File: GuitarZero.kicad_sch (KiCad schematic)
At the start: 2 parts, among them J1 AudioJack2_Ground, J2 USB_B_Micro

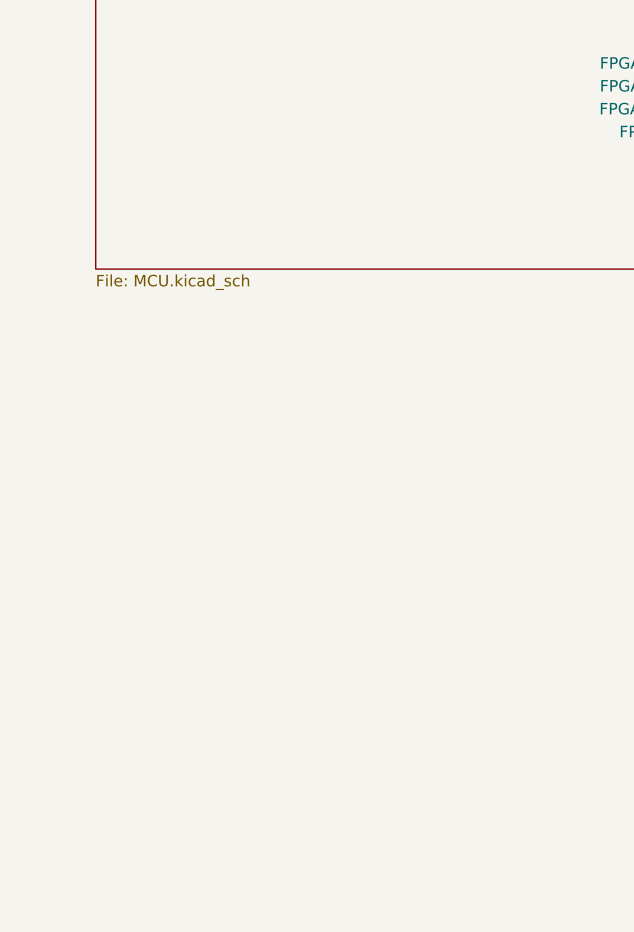
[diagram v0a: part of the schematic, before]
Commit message: Added buttons and connected them to the MCU
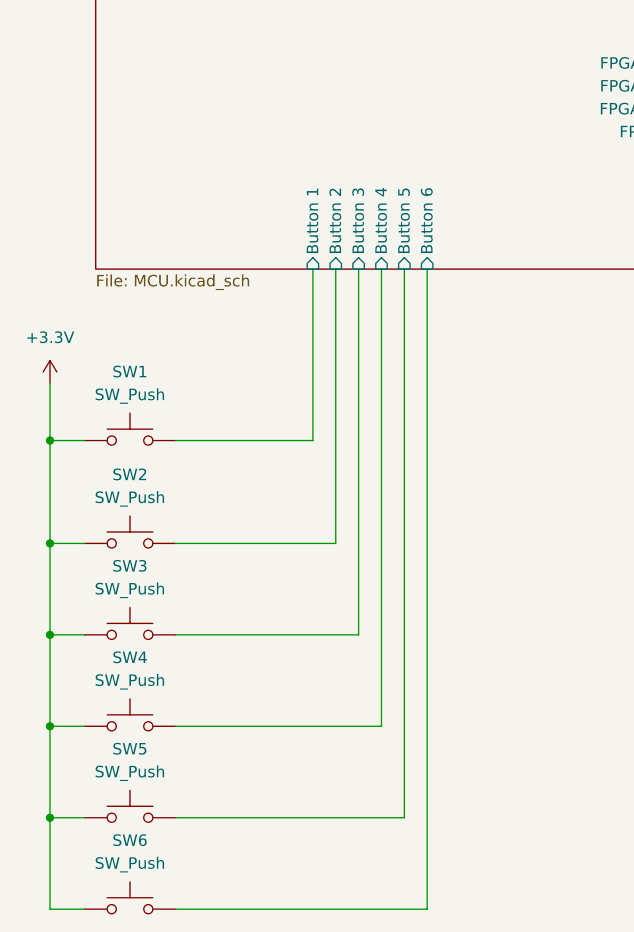
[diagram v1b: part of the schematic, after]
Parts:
- added SW1, SW2, SW3, SW4, SW5, SW6: SW_Push, symbol Switch:SW_Push
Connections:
- net +3.3V: now also SW1.1, SW2.1, SW3.1, SW4.1, SW5.1, SW6.1
- new net MCU/Button 1: SW1.2
- new net MCU/Button 2: SW2.2
- new net MCU/Button 3: SW3.2
- new net MCU/Button 4: SW4.2
- new net MCU/Button 5: SW5.2
- new net MCU/Button 6: SW6.2
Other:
- sheet MCU ports: added Button 1, Button 2, Button 3, Button 4, Button 5, Button 6; removed none

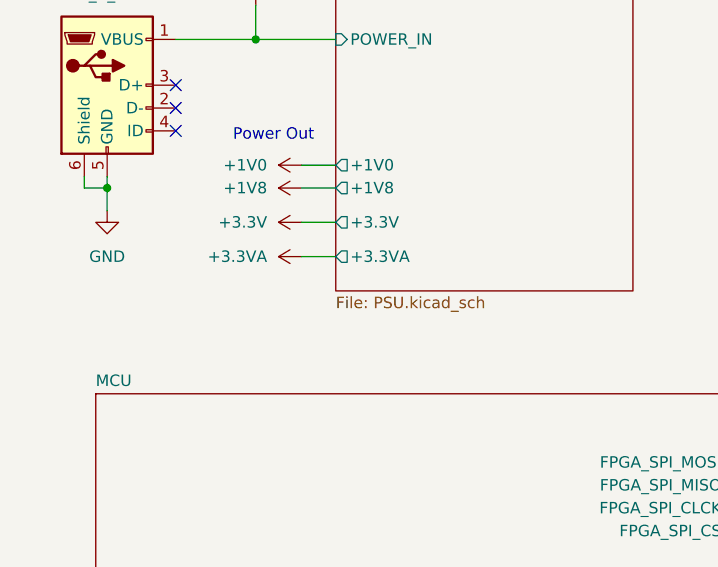
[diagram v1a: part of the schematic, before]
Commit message: Resolved some Electrial Rules
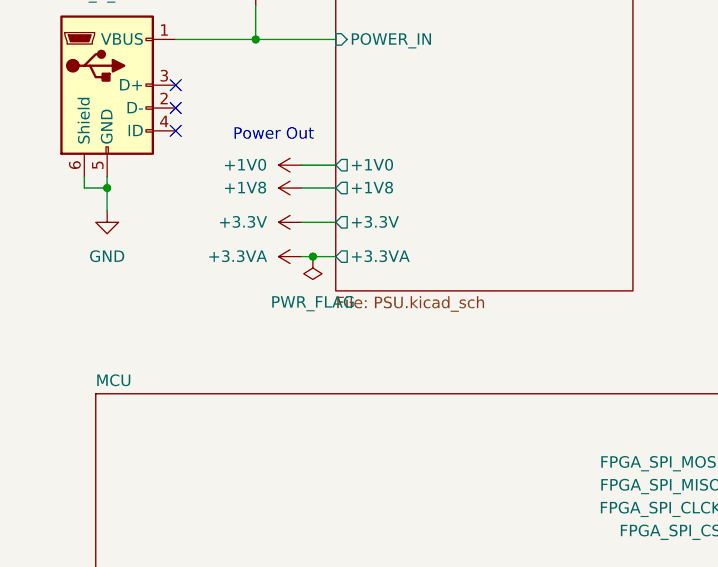
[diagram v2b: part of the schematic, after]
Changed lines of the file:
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@@
 (kicad_sch (version 20230121) (generator eeschema)
   (paper "A4")
+  (junction (at 53.34 55.88) (diameter 0) (color 0 0 0 0)
+  )
   (junction (at 24.13 120.65) (diameter 0) (color 0 0 0 0)
   )
@@
     (stroke (width 0) (type default))
   )
-  (wire (pts (xy 52.07 55.88) (xy 55.88 55.88))
+  (wire (pts (xy 52.07 55.88) (xy 53.34 55.88))
     (stroke (width 0) (type default))
   )
@@
   )
   (wire (pts (xy 55.88 132.08) (xy 55.88 101.6))
+    (stroke (width 0) (type default))
+  )
+  (wire (pts (xy 53.34 55.88) (xy 55.88 55.88))
     (stroke (width 0) (type default))
   )
@@
         )
       )
+    )
+  )
+  (symbol (lib_id "power:PWR_FLAG") (at 53.34 55.88 180) (unit 1)
+    (in_bom yes) (on_board yes) (dnp no) (fields_autoplaced)
+    (property "Reference" "#FLG01" (at 53.34 57.785 0)
+      (effects (font (size 1.27 1.27)) hide)
+    )
+    (property "Value" "PWR_FLAG" (at 53.34 60.96 0)
+      (effects (font (size 1.27 1.27)))
+    )
+    (property "Footprint" "" (at 53.34 55.88 0)
+      (effects (font (size 1.27 1.27)) hide)
+    )
+    (property "Datasheet" "~" (at 53.34 55.88 0)
+      (effects (font (size 1.27 1.27)) hide)
+    )
+    (pin "1")
+    (instances
+      (project "GuitarZero"
+        (path "/fba50eda-8593-4456-af98-ff56fd418a76"
+          (reference "#FLG01") (unit 1)
+        )
+      )

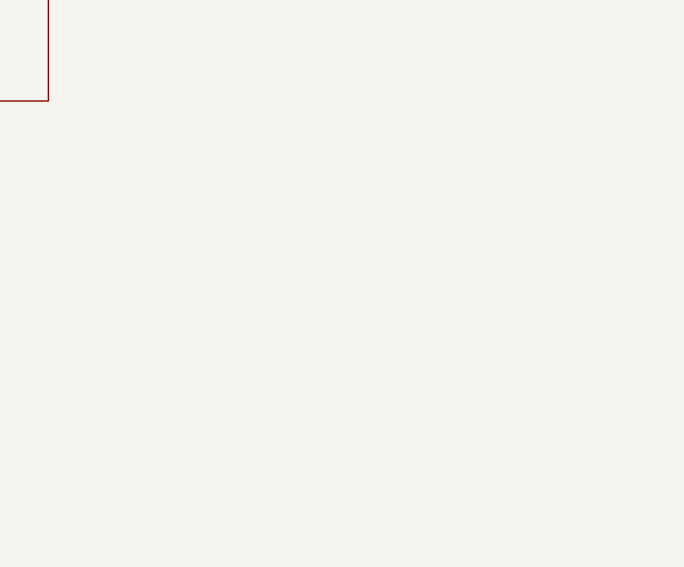
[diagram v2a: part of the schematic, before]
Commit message: Added DAC schematic
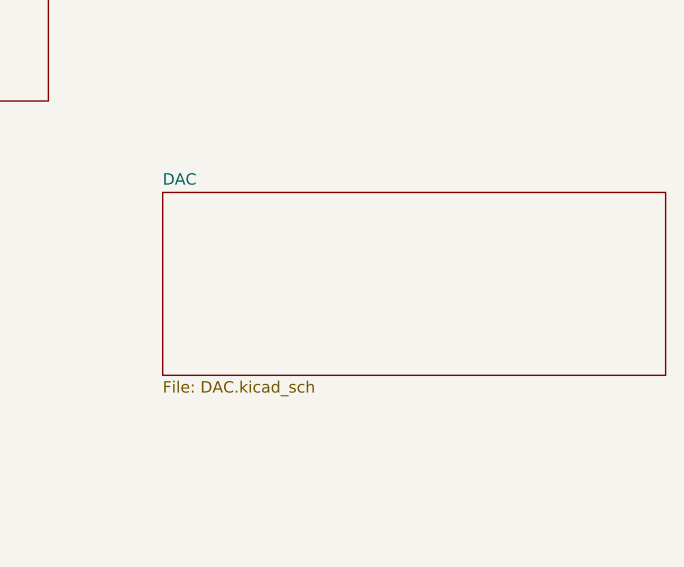
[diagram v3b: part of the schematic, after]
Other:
- added sheet DAC (DAC.kicad_sch)
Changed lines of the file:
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@@
+    )
+  )
+  (sheet (at 198.12 69.85) (size 55.88 20.32) (fields_autoplaced)
+    (stroke (width 0.1524) (type solid))
+    (fill (color 0 0 0 0.0000))
+    (property "Sheetname" "DAC" (at 198.12 69.1384 0)
+      (effects (font (size 1.27 1.27)) (justify left bottom))
+    )
+    (property "Sheetfile" "DAC.kicad_sch" (at 198.12 90.7546 0)
+      (effects (font (size 1.27 1.27)) (justify left top))
+    )
+    (instances
+      (project "GuitarZero"
+        (path "/fba50eda-8593-4456-af98-ff56fd418a76" (page "6"))
+      )
     )
   )

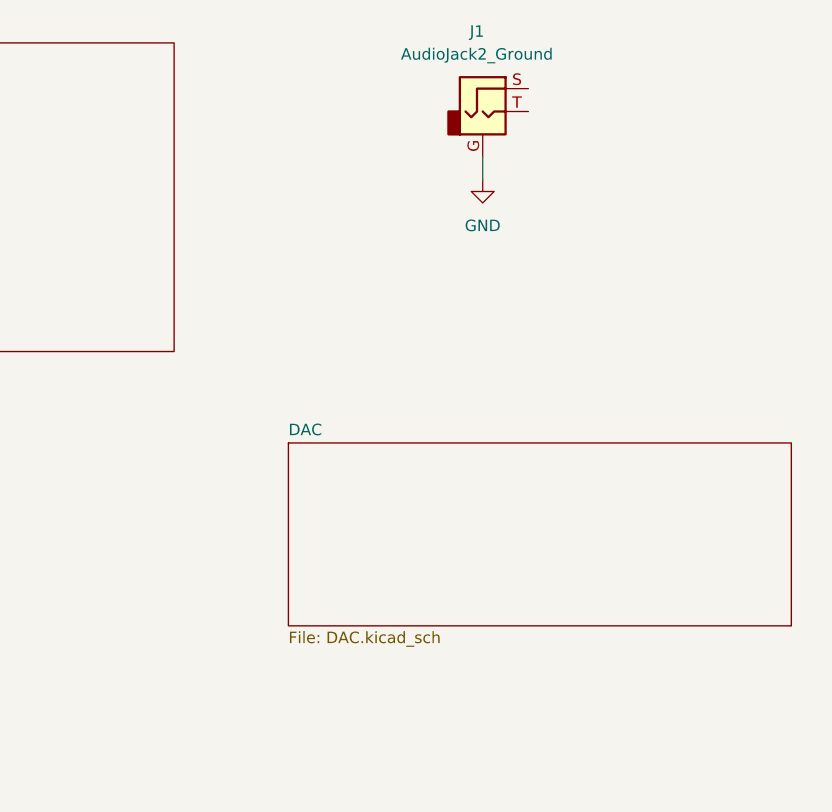
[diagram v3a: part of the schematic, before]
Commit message: Changed JACK and Speaker symbol
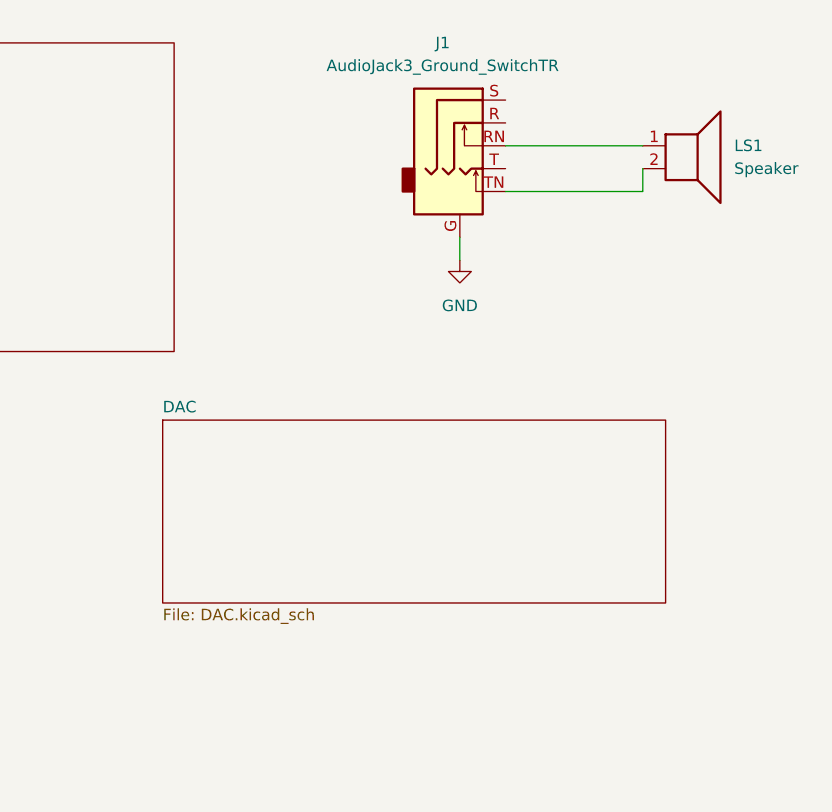
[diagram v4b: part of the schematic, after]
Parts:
- removed J1: AudioJack2_Ground, symbol Connector_Audio:AudioJack2_Ground
- added J1: AudioJack3_Ground_SwitchTR, symbol Connector_Audio:AudioJack3_Ground_SwitchTR
- added LS1: Speaker, symbol Device:Speaker
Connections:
- net GND: now also J1.G
- new net: J1.RN, LS1.1
- new net: J1.TN, LS1.2
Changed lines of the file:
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@@
+    (stroke (width 0) (type default))
+  )
+  (wire (pts (xy 237.49 41.91) (xy 237.49 39.37))
     (stroke (width 0) (type default))
   )
@@
     (stroke (width 0) (type default))
   )
+  (wire (pts (xy 222.25 41.91) (xy 237.49 41.91))
+    (stroke (width 0) (type default))
+  )
   (wire (pts (xy 24.13 120.65) (xy 24.13 132.08))
     (stroke (width 0) (type default))
@@
     (stroke (width 0) (type default))
   )
-  (wire (pts (xy 219.71 38.1) (xy 219.71 40.64))
+  (wire (pts (xy 217.17 46.99) (xy 217.17 49.53))
     (stroke (width 0) (type default))
   )
@@
   )
   (wire (pts (xy 24.13 142.24) (xy 24.13 152.4))
+    (stroke (width 0) (type default))
+  )
+  (wire (pts (xy 222.25 36.83) (xy 237.49 36.83))
     (stroke (width 0) (type default))
   )
@@
     )
   )
-  (symbol (lib_id "power:GND") (at 219.71 40.64 0) (unit 1)
-    (in_bom yes) (on_board yes) (dnp no) (fields_autoplaced)
-    (property "Reference" "#PWR033" (at 219.71 46.99 0)
-      (effects (font (size 1.27 1.27)) hide)
-    )
-    (property "Value" "GND" (at 219.71 45.72 0)
-      (effects (font (size 1.27 1.27)))
-    )
-    (property "Footprint" "" (at 219.71 40.64 0)
-      (effects (font (size 1.27 1.27)) hide)
-    )
-    (property "Datasheet" "" (at 219.71 40.64 0)
+  (symbol (lib_id "power:GND") (at 217.17 49.53 0) (unit 1)
+    (in_bom yes) (on_board yes) (dnp no) (fields_autoplaced)
+    (property "Reference" "#PWR033" (at 217.17 55.88 0)
+      (effects (font (size 1.27 1.27)) hide)
+    )
+    (property "Value" "GND" (at 217.17 54.61 0)
+      (effects (font (size 1.27 1.27)))
+    )
+    (property "Footprint" "" (at 217.17 49.53 0)
+      (effects (font (size 1.27 1.27)) hide)
+    )
+    (property "Datasheet" "" (at 217.17 49.53 0)
       (effects (font (size 1.27 1.27)) hide)
     )
@@
     )
   )
+  (symbol (lib_id "Connector_Audio:AudioJack3_Ground_SwitchTR") (at 217.17 34.29 0) (unit 1)
+    (in_bom yes) (on_board yes) (dnp no) (fields_autoplaced)
+    (property "Reference" "J1" (at 215.265 25.4 0)
+      (effects (font (size 1.27 1.27)))
+    )
+    (property "Value" "AudioJack3_Ground_SwitchTR" (at 215.265 27.94 0)
+      (effects (font (size 1.27 1.27)))
+    )
+    (property "Footprint" "" (at 217.17 34.29 0)
+      (effects (font (size 1.27 1.27)) hide)
+    )
+    (property "Datasheet" "~" (at 217.17 34.29 0)
+      (effects (font (size 1.27 1.27)) hide)
+    )
+    (pin "G")
+    (pin "R")
+    (pin "RN")
+    (pin "S")
+    (pin "T")
+    (pin "TN")
+    (instances
+      (project "GuitarZero"
+        (path "/fba50eda-8593-4456-af98-ff56fd418a76"
+          (reference "J1") (unit 1)
+        )
+      )
+    )
+  )
   (symbol (lib_id "Switch:SW_Push") (at 33.02 132.08 0) (unit 1)
     (in_bom yes) (on_board yes) (dnp no) (fields_autoplaced)
@@
         (path "/fba50eda-8593-4456-af98-ff56fd418a76"
           (reference "SW2") (unit 1)
+        )
+      )
+    )
+  )
+  (symbol (lib_id "Device:Speaker") (at 242.57 36.83 0) (unit 1)
+    (in_bom yes) (on_board yes) (dnp no) (fields_autoplaced)
+    (property "Reference" "LS1" (at 247.65 36.83 0)
+      (effects (font (size 1.27 1.27)) (justify left))
+    )
+    (property "Value" "Speaker" (at 247.65 39.37 0)
+      (effects (font (size 1.27 1.27)) (justify left))
+    )
+    (property "Footprint" "" (at 242.57 41.91 0)
+      (effects (font (size 1.27 1.27)) hide)
+    )
+    (property "Datasheet" "~" (at 242.316 38.1 0)
+      (effects (font (size 1.27 1.27)) hide)
+    )
+    (pin "1")
+    (pin "2")
+    (instances
+      (project "GuitarZero"
+        (path "/fba50eda-8593-4456-af98-ff56fd418a76"
+          (reference "LS1") (unit 1)
         )
       )
@@
     )
   )
-  (symbol (lib_id "Connector_Audio:AudioJack2_Ground") (at 219.71 33.02 0) (unit 1)
-    (in_bom yes) (on_board yes) (dnp no) (fields_autoplaced)
-    (property "Reference" "J1" (at 219.075 24.13 0)
-      (effects (font (size 1.27 1.27)))
-    )
-    (property "Value" "AudioJack2_Ground" (at 219.075 26.67 0)
-      (effects (font (size 1.27 1.27)))
-    )
-    (property "Footprint" "" (at 219.71 33.02 0)
-      (effects (font (size 1.27 1.27)) hide)
-    )
-    (property "Datasheet" "~" (at 219.71 33.02 0)
-      (effects (font (size 1.27 1.27)) hide)
-    )
-    (pin "G")
-    (pin "S")
-    (pin "T")
-    (instances
-      (project "GuitarZero"
-        (path "/fba50eda-8593-4456-af98-ff56fd418a76"
-          (reference "J1") (unit 1)
-        )
-      )
-    )
-  )
-  (sheet (at 198.12 69.85) (size 55.88 20.32) (fields_autoplaced)
+  (sheet (at 184.15 67.31) (size 55.88 20.32) (fields_autoplaced)
     (stroke (width 0.1524) (type solid))
     (fill (color 0 0 0 0.0000))
-    (property "Sheetname" "DAC" (at 198.12 69.1384 0)
+    (property "Sheetname" "DAC" (at 184.15 66.5984 0)
       (effects (font (size 1.27 1.27)) (justify left bottom))
     )
-    (property "Sheetfile" "DAC.kicad_sch" (at 198.12 90.7546 0)
+    (property "Sheetfile" "DAC.kicad_sch" (at 184.15 88.2146 0)
       (effects (font (size 1.27 1.27)) (justify left top))
     )
